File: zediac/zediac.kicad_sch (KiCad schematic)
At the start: 137 parts, among them J1 Conn_02x20_Odd_Even, J2 Conn_01x03_Male, J3 Conn_02x12_Odd_Even, J4 Conn_01x03_Male, J5 Conn_02x05_Odd_Even, J6 Conn_01x03_Male, J7 Screw_Terminal_01x02, J8 Barrel_Jack, P1 USB_C_Plug_USB2.0, Q1 Q_PMOS_GDS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

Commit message: Correct CP2102 power supply
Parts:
- R24: value 1k -> 10k
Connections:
- net VDD: now also C16.1, C18.1, U12.7 (VREGIN); no longer R25.1
- net at D3.2 (A2), J6.3 (Pin_3), P1.A4 (VBUS)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: now also R25.1; no longer C16.1, C18.1, U12.7 (VREGIN)
- net at U8.37 (~{DTRA}): now also R24.2, U12.13 (~{WAKEUP})
- no-connect marks 24 -> 23
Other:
- note added: "Address Map (Mirrored across banks): $0000-7FFF: RAM $8000-800F: VIA $8800-880F: DUART $A000-A00F: AUXCSB0 $A800-A80F: AUXCSB1 $B000-B00F: AUXCSB2 $B800-B80F: AUXCSB3 $C000-FFFF: ROM"
- note added: "NOTES: (1) VDA is not properly decoded for IO devices! This means that indexed addressing modes CANNOT be used to access IO devices on- or off-board. (2) /DTRA on the DUART can be used to wake a connected computer via USB. (3) /DSRA indicates the suspend state of the connected computer via USB."
- note added: "RAM address lines 14..0 are A14..A0 RAM address lines 18..15 are B3..B0 ROM address lines 13..0 are A13..A0 ROM address line 14 is B7"
- note added: "Wakeup resistor optional"
- company: (none) -> Electronics Tinkerer
- title: (none) -> ZEDIAC Motherboard
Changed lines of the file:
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@@
   (paper "User" 599.999 399.999)
   (title_block
-    (date "2022-10-30")
+    (title "ZEDIAC Motherboard")
+    (date "2023-01-04")
+    (rev "1.0")
+    (company "Electronics Tinkerer")
+    (comment 1 "(C) Ray Clemens 2022-2023")
   )
   (junction (at 444.5 114.3) (diameter 0) (color 0 0 0 0)
@@
   (junction (at 360.68 318.77) (diameter 0) (color 0 0 0 0)
   )
-  (junction (at 524.51 189.23) (diameter 0) (color 0 0 0 0)
-  )
   (junction (at 350.52 278.13) (diameter 0) (color 0 0 0 0)
   )
@@
   (junction (at 43.815 304.8) (diameter 0) (color 0 0 0 0)
   )
+  (junction (at 546.1 151.13) (diameter 0) (color 0 0 0 0)
+  )
   (junction (at 541.02 184.15) (diameter 0) (color 0 0 0 0)
   )
@@
   (junction (at 377.825 160.02) (diameter 0) (color 0 0 0 0)
   )
+  (junction (at 466.09 173.99) (diameter 0) (color 0 0 0 0)
+  )
   (junction (at 537.21 179.07) (diameter 0) (color 0 0 0 0)
   )
@@
   (junction (at 73.025 352.425) (diameter 0) (color 0 0 0 0)
   )
-  (junction (at 546.1 189.23) (diameter 0) (color 0 0 0 0)
-  )
   (junction (at 306.07 257.81) (diameter 0) (color 0 0 0 0)
   )
@@
   (junction (at 100.33 352.425) (diameter 0) (color 0 0 0 0)
   )
+  (junction (at 524.51 189.23) (diameter 0) (color 0 0 0 0)
+  )
   (junction (at 486.41 269.24) (diameter 0) (color 0 0 0 0)
   )
@@
   (no_connect (at 434.34 173.99))
   (no_connect (at 434.34 186.69))
-  (no_connect (at 434.34 171.45))
   (no_connect (at 472.44 196.85))
   (no_connect (at 472.44 194.31))
@@
     (stroke (width 0) (type default) (color 0 0 0 0))
   )
+  (wire (pts (xy 546.1 151.13) (xy 551.18 151.13))
+    (stroke (width 0) (type default) (color 0 0 0 0))
+  )
   (wire (pts (xy 111.76 203.2) (xy 111.76 242.57))
     (stroke (width 0) (type default) (color 0 0 0 0))
@@
     (stroke (width 0) (type default) (color 0 0 0 0))
   )
+  (wire (pts (xy 295.91 162.56) (xy 306.07 162.56))
+    (stroke (width 0) (type default) (color 0 0 0 0))
+  )
   (bus (pts (xy 134.62 130.81) (xy 134.62 133.35))
     (stroke (width 0) (type default) (color 0 0 0 0))
@@
     (stroke (width 0) (type default) (color 0 0 0 0))
   )
-  (wire (pts (xy 546.1 189.23) (xy 546.1 191.77))
+  (wire (pts (xy 546.1 166.37) (xy 546.1 191.77))
     (stroke (width 0) (type default) (color 0 0 0 0))
   )
@@
     (stroke (width 0) (type default) (color 0 0 0 0))
   )
+  (wire (pts (xy 442.595 171.45) (xy 442.595 173.99))
+    (stroke (width 0) (type default) (color 0 0 0 0))
+  )
   (wire (pts (xy 52.705 328.295) (xy 50.8 328.295))
     (stroke (width 0) (type default) (color 0 0 0 0))
@@
     (stroke (width 0) (type default) (color 0 0 0 0))
   )
+  (wire (pts (xy 434.34 171.45) (xy 442.595 171.45))
+    (stroke (width 0) (type default) (color 0 0 0 0))
+  )
   (wire (pts (xy 214.63 123.19) (xy 199.39 123.19))
     (stroke (width 0) (type default) (color 0 0 0 0))
@@
     (stroke (width 0) (type default) (color 0 0 0 0))
   )
-  (wire (pts (xy 466.09 162.56) (xy 466.09 179.07))
+  (wire (pts (xy 466.09 162.56) (xy 466.09 173.99))
     (stroke (width 0) (type default) (color 0 0 0 0))
   )
@@
     (stroke (width 0) (type default) (color 0 0 0 0))
   )
+  (wire (pts (xy 466.09 173.99) (xy 466.09 179.07))
+    (stroke (width 0) (type default) (color 0 0 0 0))
+  )
   (wire (pts (xy 182.88 247.65) (xy 187.96 247.65))
     (stroke (width 0) (type default) (color 0 0 0 0))
@@
     (stroke (width 0) (type default) (color 0 0 0 0))
   )
+  (wire (pts (xy 515.62 151.13) (xy 546.1 151.13))
+    (stroke (width 0) (type default) (color 0 0 0 0))
+  )
   (wire (pts (xy 388.62 121.92) (xy 408.94 121.92))
     (stroke (width 0) (type default) (color 0 0 0 0))
@@
     (stroke (width 0) (type default) (color 0 0 0 0))
   )
-  (wire (pts (xy 546.1 166.37) (xy 546.1 189.23))
-    (stroke (width 0) (type default) (color 0 0 0 0))
-  )
   (wire (pts (xy 539.75 162.56) (xy 546.1 162.56))
     (stroke (width 0) (type default) (color 0 0 0 0))
@@
     (stroke (width 0) (type default) (color 0 0 0 0))
   )
+  (wire (pts (xy 442.595 173.99) (xy 466.09 173.99))
+    (stroke (width 0) (type default) (color 0 0 0 0))
+  )
   (wire (pts (xy 137.16 143.51) (xy 153.67 143.51))
     (stroke (width 0) (type default) (color 0 0 0 0))
@@
     (stroke (width 0) (type default) (color 0 0 0 0))
   )
-  (wire (pts (xy 524.51 189.23) (xy 546.1 189.23))
-    (stroke (width 0) (type default) (color 0 0 0 0))
-  )
   (bus (pts (xy 37.465 241.3) (xy 37.465 248.92))
     (stroke (width 0) (type default) (color 0 0 0 0))
@@
     (stroke (width 0) (type default) (color 0 0 0 0))
   )
-  (wire (pts (xy 295.91 162.56) (xy 306.07 162.56))
-    (stroke (width 0) (type default) (color 0 0 0 0))
-  )
   (wire (pts (xy 326.39 275.59) (xy 284.48 275.59))
     (stroke (width 0) (type default) (color 0 0 0 0))
@@
     (stroke (width 0) (type default) (color 0 0 0 0))
   )
-  (wire (pts (xy 546.1 151.13) (xy 551.18 151.13))
-    (stroke (width 0) (type default) (color 0 0 0 0))
-  )
   (wire (pts (xy 546.1 162.56) (xy 546.1 166.37))
     (stroke (width 0) (type default) (color 0 0 0 0))
@@
     (stroke (width 0) (type default) (color 0 0 0 0))
   )
+  (wire (pts (xy 524.51 187.325) (xy 524.51 189.23))
+    (stroke (width 0) (type default) (color 0 0 0 0))
+  )
   (wire (pts (xy 339.09 273.05) (xy 344.17 273.05))
     (stroke (width 0) (type default) (color 0 0 0 0))
@@
     (effects (font (size 1.27 1.27)) (justify left bottom))
   )
+  (text "Wakeup resistor optional" (at 467.995 154.305 0)
+    (effects (font (size 1.27 1.27)) (justify left bottom))
+  )
   (text "ROM\nWrite\nOverride" (at 125.73 175.26 180)
     (effects (font (size 1.27 1.27)) (justify right bottom))
@@
     (effects (font (size 1.27 1.27)) (justify right bottom))
   )
+  (text "Address Map (Mirrored across banks):\n$0000-7FFF: RAM\n$8000-800F: VIA\n$8800-880F: DUART\n$A000-A00F: AUXCSB0\n$A800-A80F: AUXCSB1\n$B000-B00F: AUXCSB2\n$B800-B80F: AUXCSB3\n$C000-FFFF: ROM"
+    (at 281.94 374.015 0)
+    (effects (font (size 2.54 2.54)) (justify left bottom))
+  )
   (text "Alternate Power\nInput Regulator" (at 530.86 25.4 180)
     (effects (font (size 1.27 1.27)) (justify right bottom))
@@
     (effects (font (size 1.27 1.27)) (justify left bottom))
   )
+  (text "NOTES:\n(1) VDA is not properly decoded for IO devices! This means that indexed addressing modes CANNOT be used to access IO devices on- or off-board.\n(2) /DTRA on the DUART can be used to wake a connected computer via USB.\n(3) /DSRA indicates the suspend state of the connected computer via USB."
+    (at 63.5 35.56 0)
+    (effects (font (size 2.54 2.54)) (justify left bottom))
+  )
   (text "Reverse Polarity\nProtection\n" (at 499.745 34.925 180)
     (effects (font (size 1.27 1.27)) (justify right bottom))
   )
+  (text "RAM address lines 14..0 are A14..A0\nRAM address lines 18..15 are B3..B0\n\nROM address lines 13..0 are A13..A0\nROM address line 14 is B7"
+    (at 341.63 374.015 0)
+    (effects (font (size 2.54 2.54)) (justify left bottom))
+  )
   (text "/WRB" (at 73.025 314.96 0)
     (effects (font (size 1.27 1.27)) (justify left bottom))
@@
   (symbol (lib_id "Device:R") (at 466.09 158.75 0) (unit 1)
     (in_bom yes) (on_board yes) (fields_autoplaced)
-    (property "Reference" "R24" (id 0) (at 467.995 157.4799 0)
+    (property "Reference" "R24" (id 0) (at 468.63 157.4799 0)
       (effects (font (size 1.27 1.27)) (justify left))
     )
-    (property "Value" "1k" (id 1) (at 467.995 160.0199 0)
+    (property "Value" "10k" (id 1) (at 468.63 160.0199 0)
       (effects (font (size 1.27 1.27)) (justify left))
     )
@@
     (pin "1")
   )
-  (symbol (lib_id "zediac-logo:LOGO") (at 496.57 363.855 0) (unit 1)
+  (symbol (lib_id "zediac-logo:LOGO") (at 494.03 360.68 0) (unit 1)
     (in_bom yes) (on_board yes) (fields_autoplaced)
-    (property "Reference" "G1" (id 0) (at 496.57 362.0014 0)
+    (property "Reference" "G1" (id 0) (at 494.03 358.8264 0)
       (effects (font (size 1.27 1.27)) hide)
     )
-    (property "Value" "LOGO" (id 1) (at 496.57 365.7086 0)
+    (property "Value" "LOGO" (id 1) (at 494.03 362.5336 0)
       (effects (font (size 1.27 1.27)) hide)
     )
-    (property "Footprint" "zediac:zediac-logo" (id 2) (at 496.57 363.855 0)
+    (property "Footprint" "zediac:zediac-logo" (id 2) (at 494.03 360.68 0)
       (effects (font (size 1.27 1.27)) hide)
     )
-    (property "Datasheet" "" (id 3) (at 496.57 363.855 0)
+    (property "Datasheet" "" (id 3) (at 494.03 360.68 0)
       (effects (font (size 1.27 1.27)) hide)
     )
@@
     (pin "2")
   )
-  (symbol (lib_id "power:VDD") (at 515.62 151.13 0) (unit 1)
+  (symbol (lib_id "power:VDD") (at 524.51 187.325 0) (unit 1)
     (in_bom yes) (on_board yes)
-    (property "Reference" "#PWR071" (id 0) (at 515.62 154.94 0)
+    (property "Reference" "#PWR071" (id 0) (at 524.51 191.135 0)
       (effects (font (size 1.27 1.27)) hide)
     )
-    (property "Value" "VDD" (id 1) (at 519.43 149.86 0))
-    (property "Footprint" "" (id 2) (at 515.62 151.13 0)
+    (property "Value" "VDD" (id 1) (at 528.32 186.055 0))
+    (property "Footprint" "" (id 2) (at 524.51 187.325 0)
       (effects (font (size 1.27 1.27)) hide)
     )
-    (property "Datasheet" "" (id 3) (at 515.62 151.13 0)
+    (property "Datasheet" "" (id 3) (at 524.51 187.325 0)
       (effects (font (size 1.27 1.27)) hide)
     )
@@
     )
     (path "/9f28e98d-9a78-471a-ae98-c3943a1b1b58"
-      (reference "R24") (unit 1) (value "1k") (footprint "Resistor_SMD:R_0603_1608Metric_Pad0.98x0.95mm_HandSolder")
+      (reference "R24") (unit 1) (value "10k") (footprint "Resistor_SMD:R_0603_1608Metric_Pad0.98x0.95mm_HandSolder")
     )
     (path "/658e9c10-3eca-4339-99ef-e3e31476b6b0"

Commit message: Change USB footprint
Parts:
- P1: footprint Connector_USB:USB_C_Receptacle_Amphenol_12401548E4-2A -> custom_footprints:USB_C_Receptacle_Molex_217179-0001
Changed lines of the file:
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@@
       (effects (font (size 1.27 1.27)) (justify right))
     )
-    (property "Footprint" "Connector_USB:USB_C_Receptacle_Amphenol_12401548E4-2A" (id 2) (at 560.07 181.61 0)
+    (property "Footprint" "custom_footprints:USB_C_Receptacle_Molex_217179-0001" (id 2) (at 560.07 181.61 0)
       (effects (font (size 1.27 1.27)) hide)
     )
@@
     )
     (path "/75ca4686-7373-4b7e-a7ec-fb85333122b5"
-      (reference "P1") (unit 1) (value "USB_C_Plug_USB2.0") (footprint "Connector_USB:USB_C_Receptacle_Amphenol_12401548E4-2A")
+      (reference "P1") (unit 1) (value "USB_C_Plug_USB2.0") (footprint "custom_footprints:USB_C_Receptacle_Molex_217179-0001")
     )
     (path "/dfc09957-9bd6-492b-b089-d0f30ad4bc4d"

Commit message: Change DS1813 footprint
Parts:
- R19: value 1k -> 10k
- U2: value DS1318 -> DS1813; footprint Package_TO_SOT_THT:TO-92L_HandSolder -> Package_TO_SOT_THT:TO-92L_Wide; symbol Custom:DS1318 -> Custom:DS1813
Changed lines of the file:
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@@
   (symbol (lib_id "Device:R") (at 500.38 157.48 0) (unit 1)
     (in_bom yes) (on_board yes) (fields_autoplaced)
-    (property "Reference" "R19" (id 0) (at 502.285 156.2099 0)
+    (property "Reference" "R19" (id 0) (at 502.92 156.2099 0)
       (effects (font (size 1.27 1.27)) (justify left))
     )
-    (property "Value" "1k" (id 1) (at 502.285 158.7499 0)
+    (property "Value" "10k" (id 1) (at 502.92 158.7499 0)
       (effects (font (size 1.27 1.27)) (justify left))
     )
@@
     (pin "7")
   )
-  (symbol (lib_id "Custom:DS1318") (at 28.575 121.92 0) (unit 1)
+  (symbol (lib_id "Custom:DS1813") (at 28.575 121.92 0) (unit 1)
     (in_bom yes) (on_board yes) (fields_autoplaced)
     (property "Reference" "U2" (id 0) (at 27.94 113.03 0))
-    (property "Value" "DS1318" (id 1) (at 27.94 115.57 0))
-    (property "Footprint" "Package_TO_SOT_THT:TO-92L_HandSolder" (id 2) (at 28.575 116.84 0)
+    (property "Value" "DS1813" (id 1) (at 27.94 115.57 0))
+    (property "Footprint" "Package_TO_SOT_THT:TO-92L_Wide" (id 2) (at 28.575 116.84 0)
       (effects (font (size 1.27 1.27)) hide)
     )
@@
     )
     (path "/3c491e21-730f-4d33-90a3-2b1f3ec49ad2"
-      (reference "R19") (unit 1) (value "1k") (footprint "Resistor_SMD:R_0603_1608Metric_Pad0.98x0.95mm_HandSolder")
+      (reference "R19") (unit 1) (value "10k") (footprint "Resistor_SMD:R_0603_1608Metric_Pad0.98x0.95mm_HandSolder")
     )
     (path "/8249e76e-078a-4515-91ee-81ac27464c05"
@@
     )
     (path "/937bb1d0-c74d-43d3-9bcd-75947f52436f"
-      (reference "U2") (unit 1) (value "DS1318") (footprint "Package_TO_SOT_THT:TO-92L_HandSolder")
+      (reference "U2") (unit 1) (value "DS1813") (footprint "Package_TO_SOT_THT:TO-92L_Wide")
     )
     (path "/64ac6e46-0339-4963-8e52-c85ce7450117"

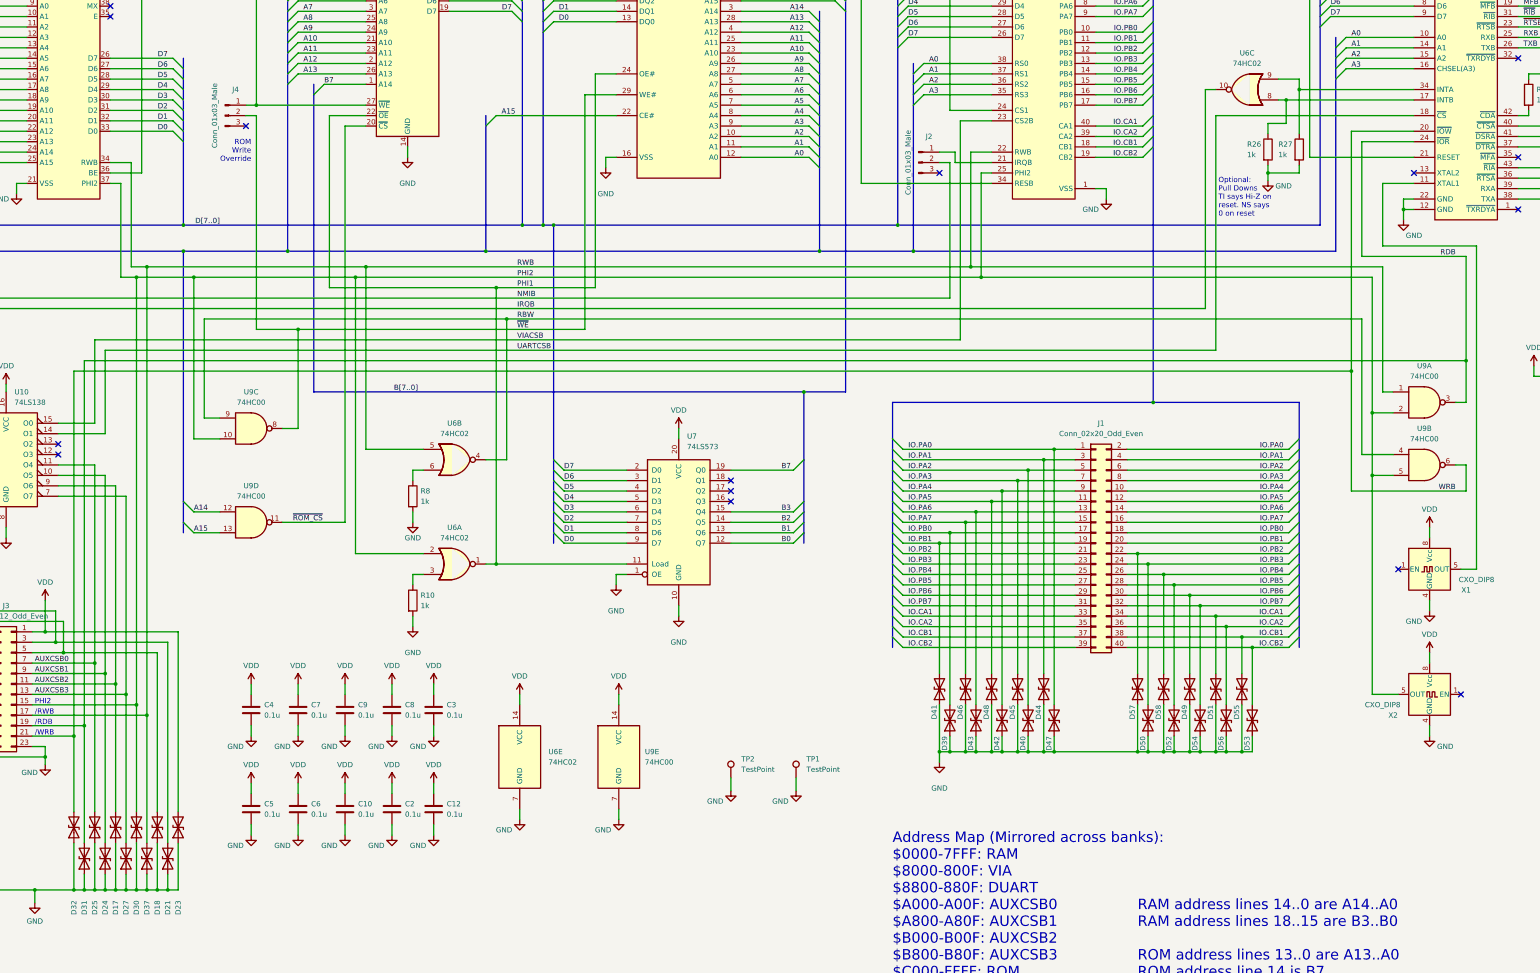
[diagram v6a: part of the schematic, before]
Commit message: [pcb] Correct EEPROM /OE signal; Remove reduandant gate; Bump Rev1.0->1.1
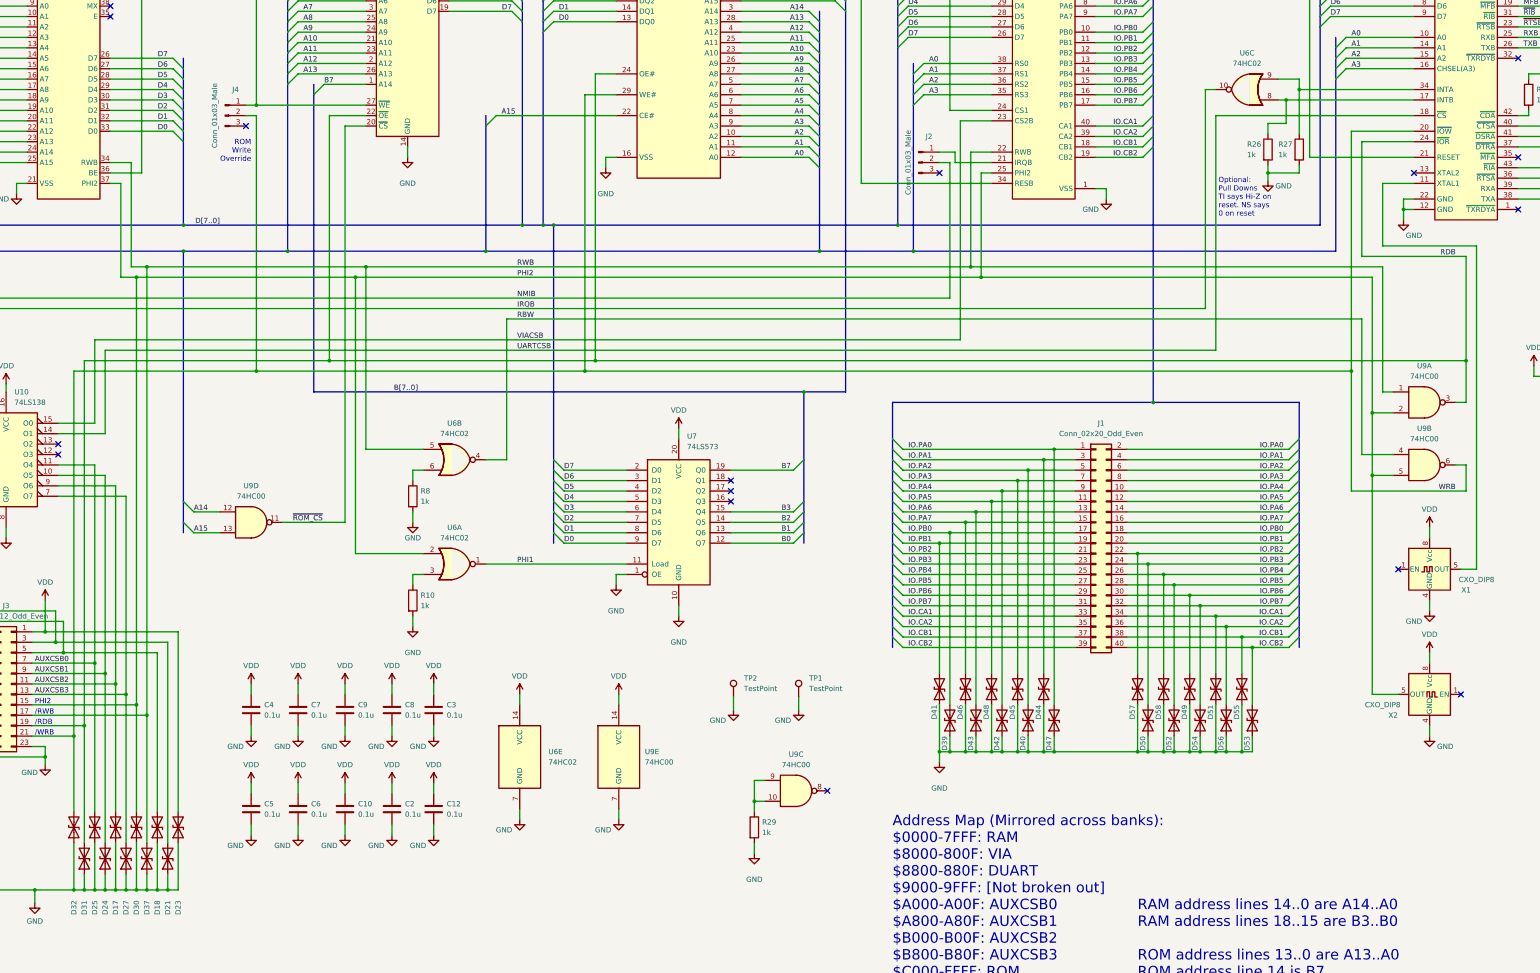
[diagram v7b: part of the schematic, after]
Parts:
- added R29: 1k, Resistor_THT:R_Axial_DIN0207_L6.3mm_D2.5mm_P7.62mm_Horizontal, symbol Device:R
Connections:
- net GND: now also R29.2
- net PHI1: no longer U4.24 (OE#), U5.22 (~{OE})
- net PHI2: no longer U9.10
- net RBW: no longer U9.9
- net RDB: now also U4.24 (OE#), U5.22 (~{OE})
- net WRB: now also J4.2 (Pin_2), U4.29 (WE#)
- removed net ~{WE}: J4.2 (Pin_2), U4.29 (WE#), U9.8
- new net: R29.1, U9.10, U9.9
- no-connect marks 23 -> 24
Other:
- note added: "Address Map (Mirrored across banks): $0000-7FFF: RAM $8000-800F: VIA $8800-880F: DUART $9000-9FFF: [Not broken out] $A000-A00F: AUXCSB0 $A800-A80F: AUXCSB1 $B000-B00F: AUXCSB2 $B800-B80F: AUXCSB3 $C000-FFFF: ROM"
- note removed: "Address Map (Mirrored across banks): $0000-7FFF: RAM $8000-800F: VIA $8800-880F: DUART $A000-A00F: AUXCSB0 $A800-A80F: AUXCSB1 $B000-B00F: AUXCSB2 $B800-B80F: AUXCSB3 $C000-FFFF: ROM"
- moved on the sheet: TP1, TP2, U9C
